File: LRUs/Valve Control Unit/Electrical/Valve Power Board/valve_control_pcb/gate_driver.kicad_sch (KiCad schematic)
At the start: 15 parts, among them U14 UCC27524D, U15 UCC27524D, U16 UCC27524D

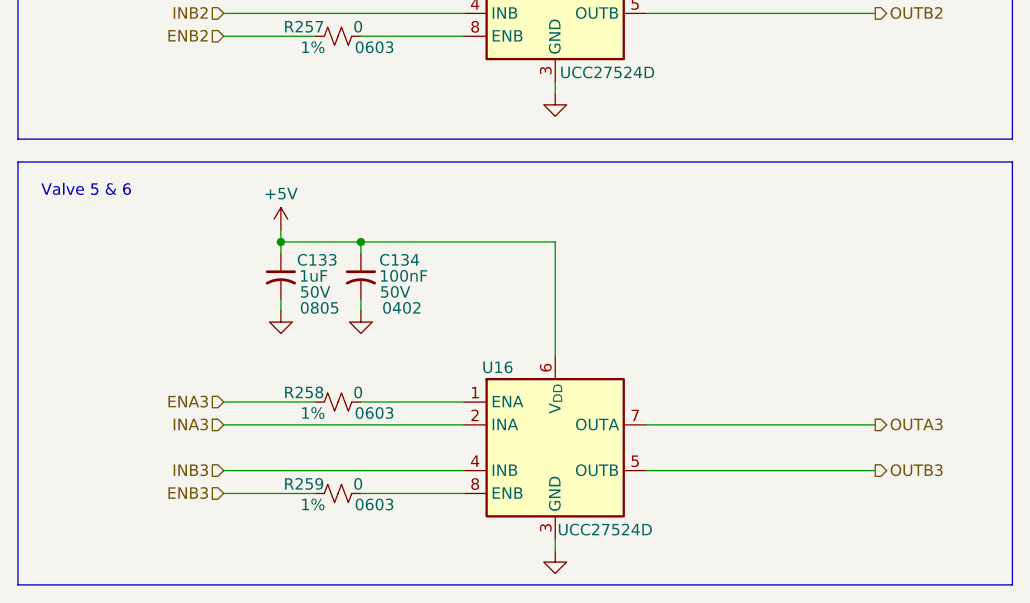
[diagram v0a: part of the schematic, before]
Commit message: Major changes due to architecture
Added battery muxing for valve power, igniter system, and separate system battery for control electronics
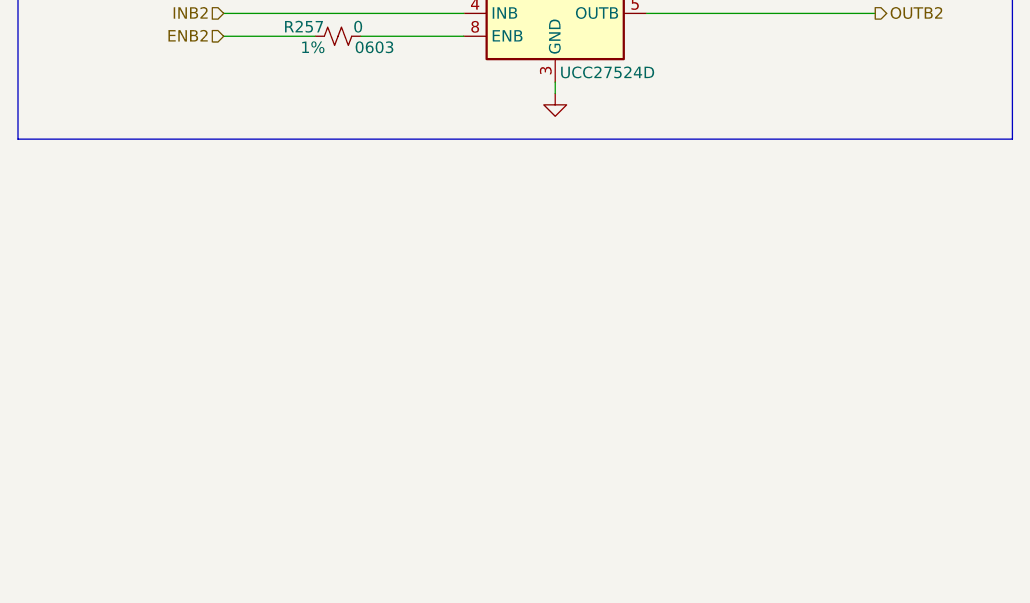
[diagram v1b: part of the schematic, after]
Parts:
- removed C133: 1uF, valve_pcb_footprints:C_0805_2012Metric, symbol Device:C_Small_US
- removed C134: 100nF, valve_pcb_footprints:C_0402_1005Metric, symbol Device:C_Small_US
- removed R258, R259: 0, valve_pcb_footprints:R_0603_1608Metric, symbol Device:R_Small_US
- removed U16: UCC27524D, Package_SO:SOIC-8_3.9x4.9mm_P1.27mm, symbol Driver_FET:UCC27524D
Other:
- note removed: "Valve 5 & 6"

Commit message: Small updates
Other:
- moved on the sheet: C129, C130, C131, C132, R254, R255, R256, R257, U14, U15

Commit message: Fixes
Added hops, fixed the planes, and fixed minor issues
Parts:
- renumbered C130 to C40, C131 to C41, C129 to C42, C132 to C43, R254 to R50, R255 to R51, R256 to R52, R257 to R53, U14 to U10, U15 to U11
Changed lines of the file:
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@@
 		(in_pos_files yes)
 		(dnp no)
-		(property "Reference" "C130"
+		(property "Reference" "C40"
 			(at 124.968 54.102 0)
 			(show_name no)
@@
 			(project "valve_control_pcb"
 				(path "/d4e8203a-d76f-4c3b-b909-1a52c35190e7/1014ec9d-d2d6-4589-8472-e64627808162"
-					(reference "C130")
+					(reference "C40")
 					(unit 1)
 					(variant
@@
 		(in_pos_files yes)
 		(dnp no)
-		(property "Reference" "C132"
+		(property "Reference" "C43"
 			(at 135.382 103.632 0)
 			(show_name no)
@@
 			(project "valve_control_pcb"
 				(path "/d4e8203a-d76f-4c3b-b909-1a52c35190e7/1014ec9d-d2d6-4589-8472-e64627808162"
-					(reference "C132")
+					(reference "C43")
 					(unit 1)
 					(variant
@@
 		(in_pos_files yes)
 		(dnp no)
-		(property "Reference" "U15"
+		(property "Reference" "U11"
 			(at 146.812 115.57 0)
 			(show_name no)
@@
 			(project "valve_control_pcb"
 				(path "/d4e8203a-d76f-4c3b-b909-1a52c35190e7/1014ec9d-d2d6-4589-8472-e64627808162"
-					(reference "U15")
+					(reference "U11")
 					(unit 1)
 				)
@@
 		(in_pos_files yes)
 		(dnp no)
-		(property "Reference" "#PWR0275"
+		(property "Reference" "#PWR075"
 			(at 124.46 104.14 0)
 			(hide yes)
@@
 			(project "valve_control_pcb"
 				(path "/d4e8203a-d76f-4c3b-b909-1a52c35190e7/1014ec9d-d2d6-4589-8472-e64627808162"
-					(reference "#PWR0275")
+					(reference "#PWR075")
 					(unit 1)
 				)
@@
 		(in_pos_files yes)
 		(dnp no)
-		(property "Reference" "C131"
+		(property "Reference" "C41"
 			(at 126.238 103.632 0)
 			(show_name no)
@@
 			(project "valve_control_pcb"
 				(path "/d4e8203a-d76f-4c3b-b909-1a52c35190e7/1014ec9d-d2d6-4589-8472-e64627808162"
-					(reference "C131")
+					(reference "C41")
 					(unit 1)
 					(variant
@@
 		(in_pos_files yes)
 		(dnp no)
-		(property "Reference" "#PWR0174"
+		(property "Reference" "#PWR073"
 			(at 123.19 54.61 0)
 			(hide yes)
@@
 			(project "valve_control_pcb"
 				(path "/d4e8203a-d76f-4c3b-b909-1a52c35190e7/1014ec9d-d2d6-4589-8472-e64627808162"
-					(reference "#PWR0174")
+					(reference "#PWR073")
 					(unit 1)
 				)
@@
 		(in_pos_files yes)
 		(dnp no)
-		(property "Reference" "U14"
+		(property "Reference" "U10"
 			(at 145.796 66.04 0)
 			(show_name no)
@@
 			(project "valve_control_pcb"
 				(path "/d4e8203a-d76f-4c3b-b909-1a52c35190e7/1014ec9d-d2d6-4589-8472-e64627808162"
-					(reference "U14")
+					(reference "U10")
 					(unit 1)
 				)
@@
 		(in_pos_files yes)
 		(dnp no)
-		(property "Reference" "R257"
+		(property "Reference" "R53"
 			(at 129.286 128.524 90)
 			(show_name no)
@@
 			(project "valve_control_pcb"
 				(path "/d4e8203a-d76f-4c3b-b909-1a52c35190e7/1014ec9d-d2d6-4589-8472-e64627808162"
-					(reference "R257")
+					(reference "R53")
 					(unit 1)
 					(variant
@@
 		(dnp no)
 		(fields_autoplaced yes)
-		(property "Reference" "#PWR0320"
+		(property "Reference" "#PWR076"
 			(at 124.46 115.57 0)
 			(hide yes)
@@
 			(project "valve_control_pcb"
 				(path "/d4e8203a-d76f-4c3b-b909-1a52c35190e7/1014ec9d-d2d6-4589-8472-e64627808162"
-					(reference "#PWR0320")
+					(reference "#PWR076")
 					(unit 1)
 				)
@@
 		(dnp no)
 		(fields_autoplaced yes)
-		(property "Reference" "#PWR0323"
+		(property "Reference" "#PWR078"
 			(at 133.35 115.57 0)
 			(hide yes)
@@
 			(project "valve_control_pcb"
 				(path "/d4e8203a-d76f-4c3b-b909-1a52c35190e7/1014ec9d-d2d6-4589-8472-e64627808162"
-					(reference "#PWR0323")
+					(reference "#PWR078")
 					(unit 1)
 				)
@@
 		(in_pos_files yes)
 		(dnp no)
-		(property "Reference" "R256"
+		(property "Reference" "R52"
 			(at 129.286 118.364 90)
 			(show_name no)
@@
 			(project "valve_control_pcb"
 				(path "/d4e8203a-d76f-4c3b-b909-1a52c35190e7/1014ec9d-d2d6-4589-8472-e64627808162"
-					(reference "R256")
+					(reference "R52")
 					(unit 1)
 					(variant
@@
 		(in_pos_files yes)
 		(dnp no)
-		(property "Reference" "C129"
+		(property "Reference" "C42"
 			(at 134.112 54.102 0)
 			(show_name no)
@@
 			(project "valve_control_pcb"
 				(path "/d4e8203a-d76f-4c3b-b909-1a52c35190e7/1014ec9d-d2d6-4589-8472-e64627808162"
-					(reference "C129")
+					(reference "C42")
 					(unit 1)
 					(variant
@@
 		(dnp no)
 		(fields_autoplaced yes)
-		(property "Reference" "#PWR0173"
+		(property "Reference" "#PWR074"
 			(at 123.19 66.04 0)
 			(hide yes)
@@
 			(project "valve_control_pcb"
 				(path "/d4e8203a-d76f-4c3b-b909-1a52c35190e7/1014ec9d-d2d6-4589-8472-e64627808162"
-					(reference "#PWR0173")
+					(reference "#PWR074")
 					(unit 1)
 				)
@@
 		(in_pos_files yes)
 		(dnp no)
-		(property "Reference" "R254"
+		(property "Reference" "R50"
 			(at 128.016 68.834 90)
 			(show_name no)
@@
 			(project "valve_control_pcb"
 				(path "/d4e8203a-d76f-4c3b-b909-1a52c35190e7/1014ec9d-d2d6-4589-8472-e64627808162"
-					(reference "R254")
+					(reference "R50")
 					(unit 1)
 					(variant
@@
 		(dnp no)
 		(fields_autoplaced yes)
-		(property "Reference" "#PWR0319"
+		(property "Reference" "#PWR079"
 			(at 153.67 92.71 0)
 			(hide yes)
@@
 			(project "valve_control_pcb"
 				(path "/d4e8203a-d76f-4c3b-b909-1a52c35190e7/1014ec9d-d2d6-4589-8472-e64627808162"
-					(reference "#PWR0319")
+					(reference "#PWR079")
 					(unit 1)
 				)
@@
 		(in_pos_files yes)
 		(dnp no)
-		(property "Reference" "R255"
+		(property "Reference" "R51"
 			(at 128.016 78.994 90)
 			(show_name no)
@@
 			(project "valve_control_pcb"
 				(path "/d4e8203a-d76f-4c3b-b909-1a52c35190e7/1014ec9d-d2d6-4589-8472-e64627808162"
-					(reference "R255")
+					(reference "R51")
 					(unit 1)
 					(variant
@@
 		(dnp no)
 		(fields_autoplaced yes)
-		(property "Reference" "#PWR0321"
+		(property "Reference" "#PWR080"
 			(at 154.94 142.24 0)
 			(hide yes)
@@
 			(project "valve_control_pcb"
 				(path "/d4e8203a-d76f-4c3b-b909-1a52c35190e7/1014ec9d-d2d6-4589-8472-e64627808162"
-					(reference "#PWR0321")
+					(reference "#PWR080")
 					(unit 1)
 				)
@@
 		(dnp no)
 		(fields_autoplaced yes)
-		(property "Reference" "#PWR0322"
+		(property "Reference" "#PWR077"
 			(at 132.08 66.04 0)
 			(hide yes)
@@
 			(project "valve_control_pcb"
 				(path "/d4e8203a-d76f-4c3b-b909-1a52c35190e7/1014ec9d-d2d6-4589-8472-e64627808162"
-					(reference "#PWR0322")
+					(reference "#PWR077")
 					(unit 1)
 				)

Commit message: Delete a bunch of stuff
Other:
- note added: "GATE DRIVERS"
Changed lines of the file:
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@@
+		)
+	)
+	(text "GATE DRIVERS"
+		(exclude_from_sim no)
+		(at 146.05 31.242 0)
+		(effects
+			(font
+				(size 7.62 7.62)
+				(thickness 1.016)
+				(bold yes)
+				(color 0 0 0 1)
+			)
 		)
 	)
